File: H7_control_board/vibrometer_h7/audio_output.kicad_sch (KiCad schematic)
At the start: 21 parts, among them J2 AudioJack3, U6 TPA6111A2

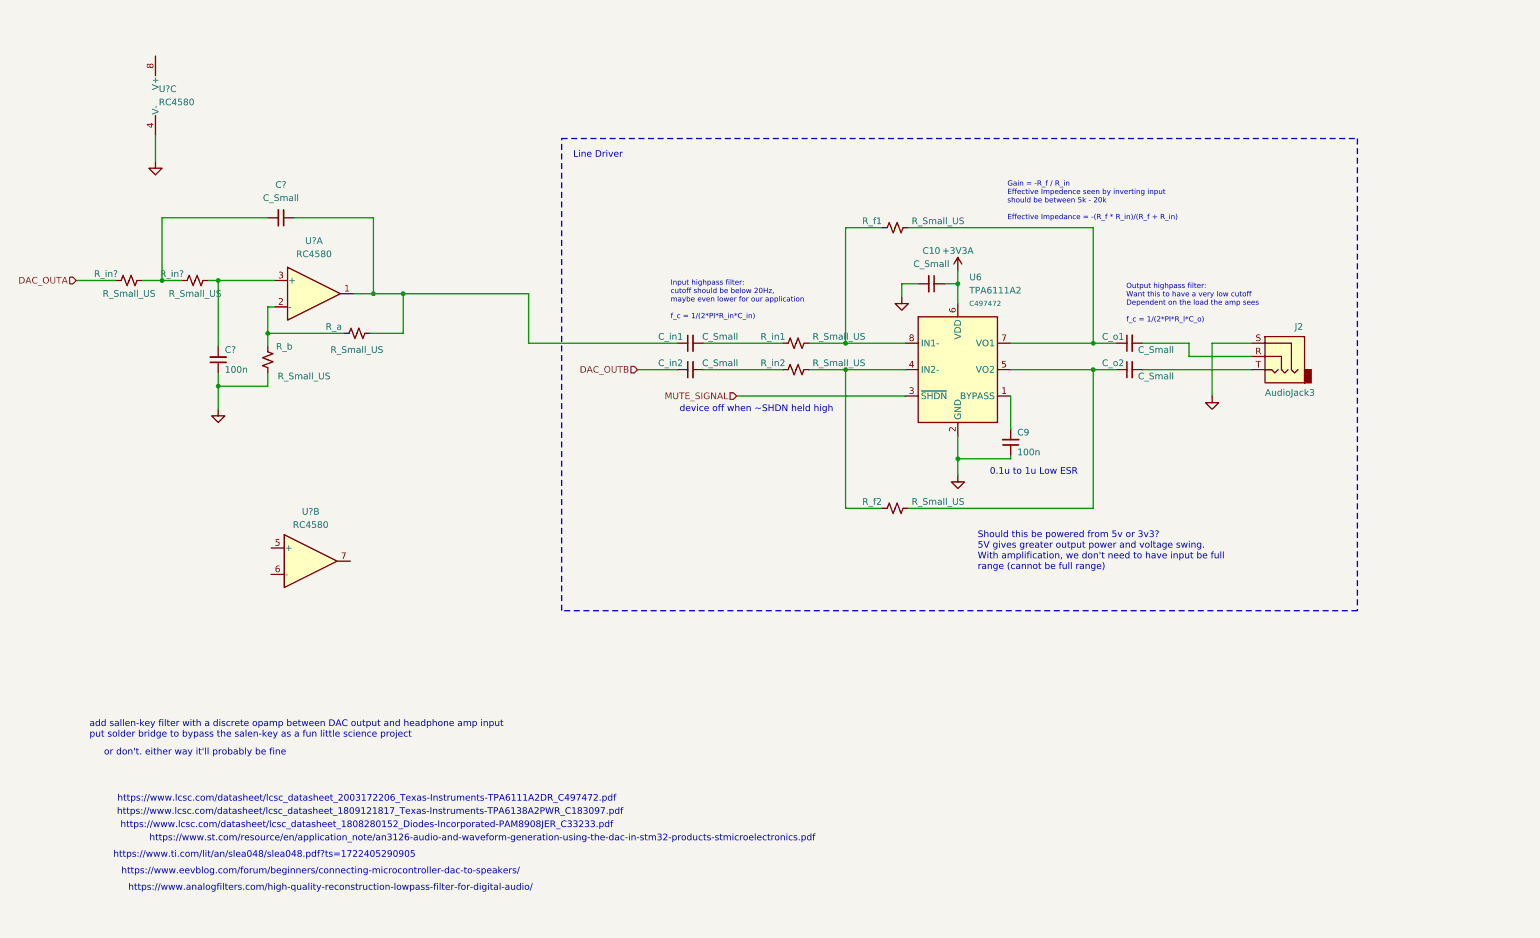
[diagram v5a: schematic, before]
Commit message: component selection, headphone amp circuit specs
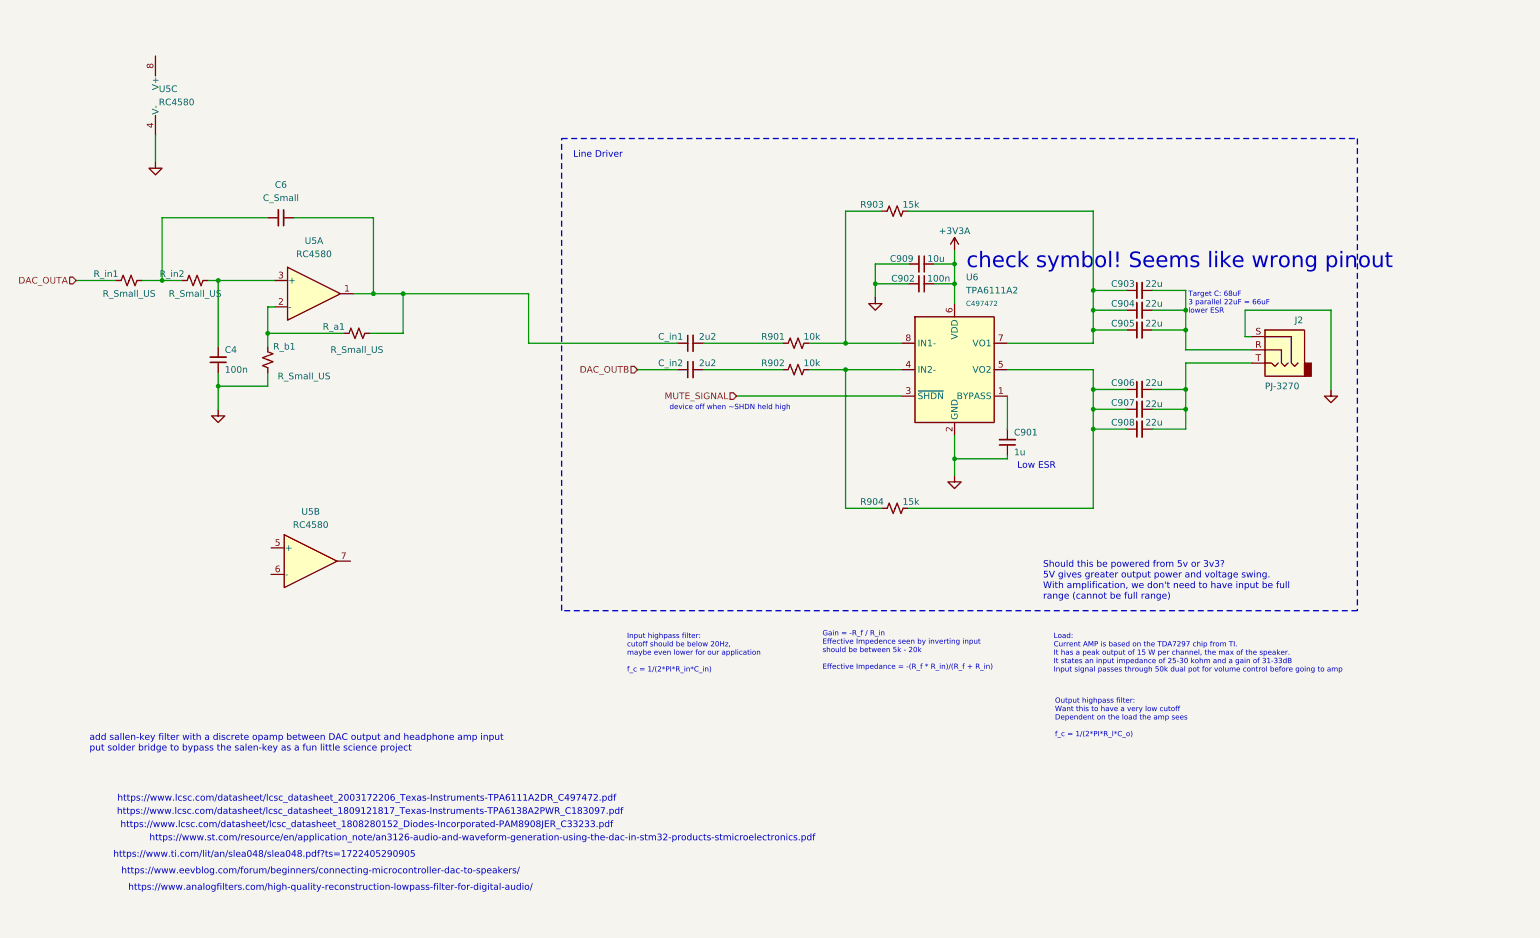
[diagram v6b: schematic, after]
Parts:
- added C904, C905, C906, C908: 22u, Capacitor_SMD:C_0805_2012Metric, symbol Device:C_Small
- added C909: 10u, Capacitor_SMD:C_0805_2012Metric, symbol Device:C_Small
- C4: renamed from C?; footprint Capacitor_SMD:C_0603_1608Metric -> Capacitor_SMD:C_0402_1005Metric_Pad0.74x0.62mm_HandSolder; LCSC (none) -> C307331
- C901: renamed from C9; value 100n -> 1u; footprint Capacitor_SMD:C_0603_1608Metric -> Capacitor_SMD:C_0805_2012Metric; LCSC (none) -> C28323
- C902: renamed from C10; value C_Small -> 100n; LCSC (none) -> C307331
- C903: renamed from C_o1; value C_Small -> 22u; footprint Capacitor_SMD:C_0603_1608Metric -> Capacitor_SMD:C_0805_2012Metric; LCSC (none) -> C45783
- C907: renamed from C_o2; value C_Small -> 22u; footprint Capacitor_SMD:C_0603_1608Metric -> Capacitor_SMD:C_0805_2012Metric; LCSC (none) -> C45783
- C_in1, C_in2: value C_Small -> 2u2; footprint Capacitor_SMD:C_0603_1608Metric -> Capacitor_SMD:C_0805_2012Metric; LCSC (none) -> C377773
- J2: value AudioJack3 -> PJ-3270; footprint (none) -> footprints:AUDIO-TH_PJ-3270; LCSC (none) -> C381134
- R901: renamed from R_in1; value R_Small_US -> 10k
- R902: renamed from R_in2; value R_Small_US -> 10k
- R903: renamed from R_f1; value R_Small_US -> 15k
- R904: renamed from R_f2; value R_Small_US -> 15k
- gave numbers to parts that had none: 4
- renumbered R_a to R_a1, R_b to R_b1
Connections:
- net +3V3A: now also C909.1
- net GND: now also C909.2
- net at C903.1, R903.2, U6.7 (VO1): now also C904.1, C905.1
- net at C903.2, J2.R: now also C904.2, C905.2
- net at C907.2, J2.T: now also C906.2, C908.2
- net at C907.1, R904.2, U6.5 (VO2): now also C906.1, C908.1
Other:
- note added: "Load: Current AMP is based on the TDA7297 chip from TI. It has a peak output of 15 W per channel, the max of the speaker. It states an input impedance of 25-30 kohm and a gain of 31-33dB Input signal passes through 50k dual pot for volume control before going to amp"
- note added: "Low ESR"
- note added: "Target C: 68uF 3 parallel 22uF = 66uF lower ESR"
- note added: "check symbol! Seems like wrong pinout"
- note removed: "0.1u to 1u Low ESR"
- note removed: "or don't. either way it'll probably be fine"
- moved on the sheet: C901, C902, C903, C907, J2, R903, U6

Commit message: part selection for audio, schematic cleanup
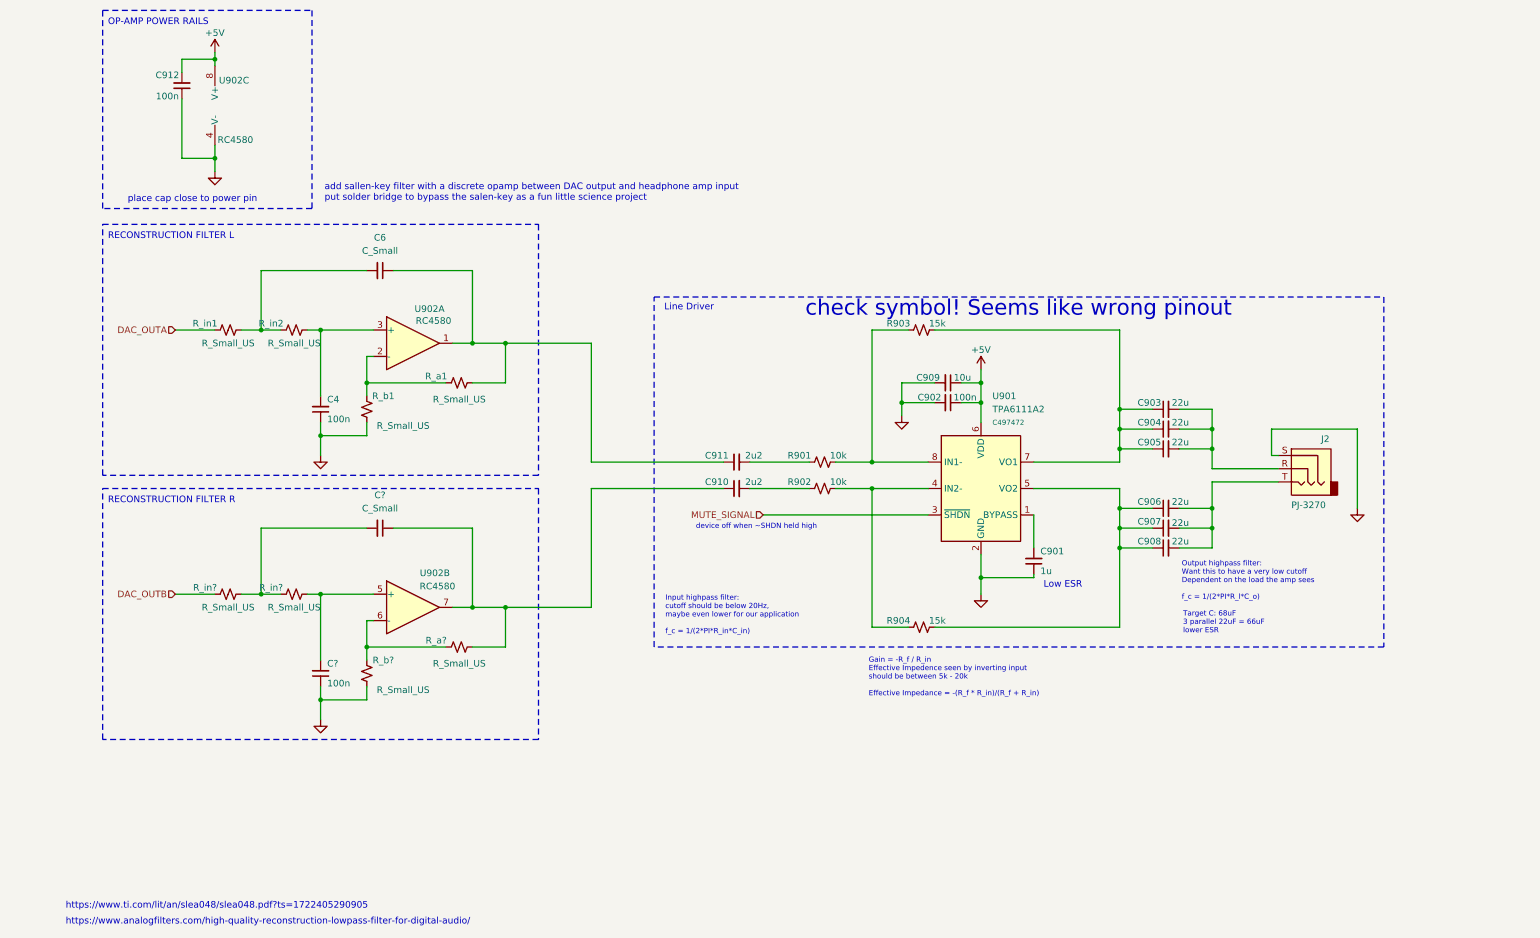
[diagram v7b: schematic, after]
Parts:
- added C912: 100n, Capacitor_SMD:C_0603_1608Metric, symbol Device:C_Small
- added C?: C_Small, Capacitor_SMD:C_0603_1608Metric, symbol Device:C_Small
- added C?: 100n, Capacitor_SMD:C_0402_1005Metric_Pad0.74x0.62mm_HandSolder, symbol Device:C_Small
- added R_a?, R_b?, R_in? (x2): R_Small_US, symbol Device:R_Small_US
- R901, R902: footprint (none) -> Resistor_SMD:R_0805_2012Metric; LCSC (none) -> C17414
- R903, R904: footprint (none) -> Resistor_SMD:R_0805_2012Metric; LCSC (none) -> C17475
- renumbered C_in2 to C910, C_in1 to C911, U6 to U901, U5 to U902
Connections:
- net +3V3A is gone; now on net +5V: C902.1, C909.1, U901.6 (VDD)
- net DAC_OUTB: now also R_in?.1; no longer C910.1
- net GND: now also C912.1, C?.1, R_b?.1
- net +5V: now reaches U902.8 (V+)
- net +5V: now also C912.2
- net at U902.5 (+): now also C?.2, R_in?.2
- net at U902.6 (-): now also R_a?.1, R_b?.2
- net at U902.7: now also C910.1, C?.1, R_a?.2
- new net: C?.2, R_in?.1, R_in?.2
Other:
- note added: "OP-AMP POWER RAILS"
- note added: "RECONSTRUCTION FILTER L"
- note added: "RECONSTRUCTION FILTER R"
- note added: "place cap close to power pin"
- note removed: "Load: Current AMP is based on the TDA7297 chip from TI. It has a peak output of 15 W per channel, the max of the speaker. It states an input impedance of 25-30 kohm and a gain of 31-33dB Input signal passes through 50k dual pot for volume control before going to amp"
- note removed: "Should this be powered from 5v or 3v3? 5V gives greater output power and voltage swing. With amplification, we don't need to have input be full range (cannot be full range)"
- note removed: "https://www.eevblog.com/forum/beginners/connecting-microcontroller-dac-to-speakers/"
- note removed: "https://www.lcsc.com/datasheet/lcsc_datasheet_1808280152_Diodes-Incorporated-PAM8908JER_C33233.pdf"
- note removed: "https://www.lcsc.com/datasheet/lcsc_datasheet_1809121817_Texas-Instruments-TPA6138A2PWR_C183097.pdf"
- note removed: "https://www.lcsc.com/datasheet/lcsc_datasheet_2003172206_Texas-Instruments-TPA6111A2DR_C497472.pdf"
- note removed: "https://www.st.com/resource/en/application_note/an3126-audio-and-waveform-generation-using-the-dac-in-stm32-products-stmicroelectronics.pdf"
- moved on the sheet: C4, C6, C901, C902, C903, C904, C905, C906, C907, C908, C909, C910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

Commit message: updated reference designator naming
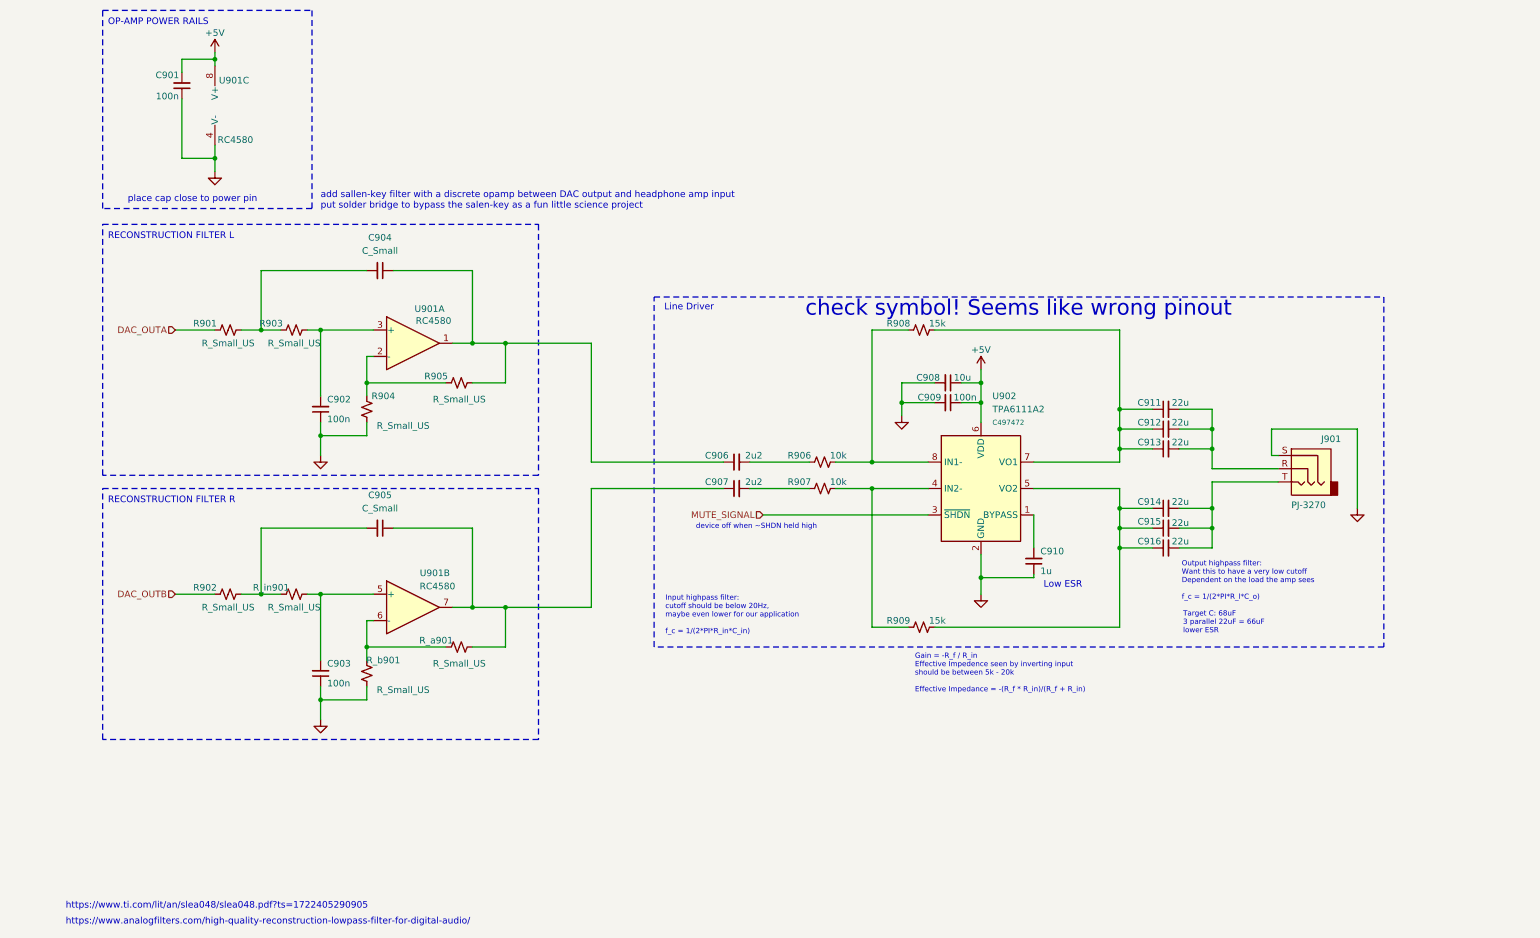
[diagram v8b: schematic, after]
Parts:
- gave numbers to parts that had none: 6
- renumbered C912 to C901, C4 to C902, C6 to C904, C911 to C906, C910 to C907, C909 to C908, C902 to C909, C901 to C910, C903 to C911, C904 to C912, C905 to C913, C906 to C914, C907 to C915, C908 to C916, J2 to J901, R_in1 to R901, R_in2 to R903, R_b1 to R904, R_a1 to R905, R901 to R906, R902 to R907, R903 to R908, R904 to R909, U902 to U901, U901 to U902
